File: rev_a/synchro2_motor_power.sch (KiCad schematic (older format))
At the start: 39 parts, among them U10 OPTOISOLATOR2, U11 OPTOISOLATOR2, U12 74XX74, U13 L298, U14 L298, U15 MCP48X2, U16 MCP6542, U7 LM2931, U8 SI8420, U9 SI8420

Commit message: Rev. A is pretty close to being ready.
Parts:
- added TP10: DAC_AOUT, symbol TEST_POINT
- added TP11: TWEN, symbol TEST_POINT
- added TP12: TW_SEN, symbol TEST_POINT
- added TP4: PWM_CLK, symbol TEST_POINT
- added TP5: MPWR, symbol TEST_POINT
- added TP6: MGND, symbol TEST_POINT
- added TP7: DAC_SDI, symbol TEST_POINT
- added TP8: DAC_SCK, symbol TEST_POINT
- added TP9: DAC_CS, symbol TEST_POINT
- C13: renamed from C12; value C -> 22uF
- C18: renamed from C17; value .uF -> .1uF
- U10, U11: value OPTOISOLATOR2 -> ELD207
- renumbered C13 to C14, C14 to C15, C15 to C16, C16 to C17, C18 to C19, C19 to C20, C20 to C21, N4 to N5, N5 to N6
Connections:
- net MB_MGND: now also TP6.1 (TESTPOINT)
- net MB_MPWR: now also TP5.1 (TESTPOINT)
- net TW_SEN: now reaches R12.2, U13.1 (CSA), U13.15 (CSB), U16.6
- net TW_SEN: now also TP12.1 (TESTPOINT)
- net TWD2: now reaches R9.1, U10.6, U13.10 (IN3), U13.7 (IN2)
- net TWEN: now reaches U12.9, U13.11 (EN1), U13.6 (EN2)
- net TWEN: now also TP11.1 (TESTPOINT)
- net TWD1: now reaches R7.1, U10.8, U13.12 (IN4), U13.5 (IN1)
- net TW-: now reaches D2.2 (CATHODE), D3.1 (ANODE), N5.2 (-), U13.13 (OUT3), U13.3 (OUT2)
- net TW+: now reaches D6.2 (CATHODE), D7.1 (ANODE), N5.1 (+), U13.14 (OUT4), U13.2 (OUT1)
- net DR_SEN: now reaches R11.2, U14.1 (CSA), U14.15 (CSB), U16.2
- net DRD2: now reaches R10.1, U11.6, U14.10 (IN3), U14.7 (IN2)
- net DREN: now reaches U12.5, U14.11 (EN1), U14.6 (EN2)
- net DRD1: now reaches R8.1, U11.8, U14.12 (IN4), U14.5 (IN1)
- net DR-: now reaches D4.2 (CATHODE), D5.1 (ANODE), N6.2 (-), U14.13 (OUT3), U14.3 (OUT2)
- net DR+: now reaches D8.2 (CATHODE), D9.1 (ANODE), N6.1 (+), U14.14 (OUT4), U14.2 (OUT1)
- net at U15.8 (VOUTA), U16.5: now also TP10.1 (TESTPOINT)
- net at U12.11, U12.3, U8.7 (B1): now also TP4.1 (TESTPOINT)
- net at U15.2 (~CS), U8.6 (B2): now also TP9.1 (TESTPOINT)
- net at U15.3 (SCK), U9.7 (B1): now also TP8.1 (TESTPOINT)
- net at U15.4 (SDI), U9.6 (B2): now also TP7.1 (TESTPOINT)
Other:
- note added: "+\n"
- note added: "35V Alum."
- note added: "6.3V Tant."
- note added: "AVX: TAJA226K006RNJ"
- note added: "KMet: EEV226M035A9DAA"
- moved on the sheet: N5, N6, R12

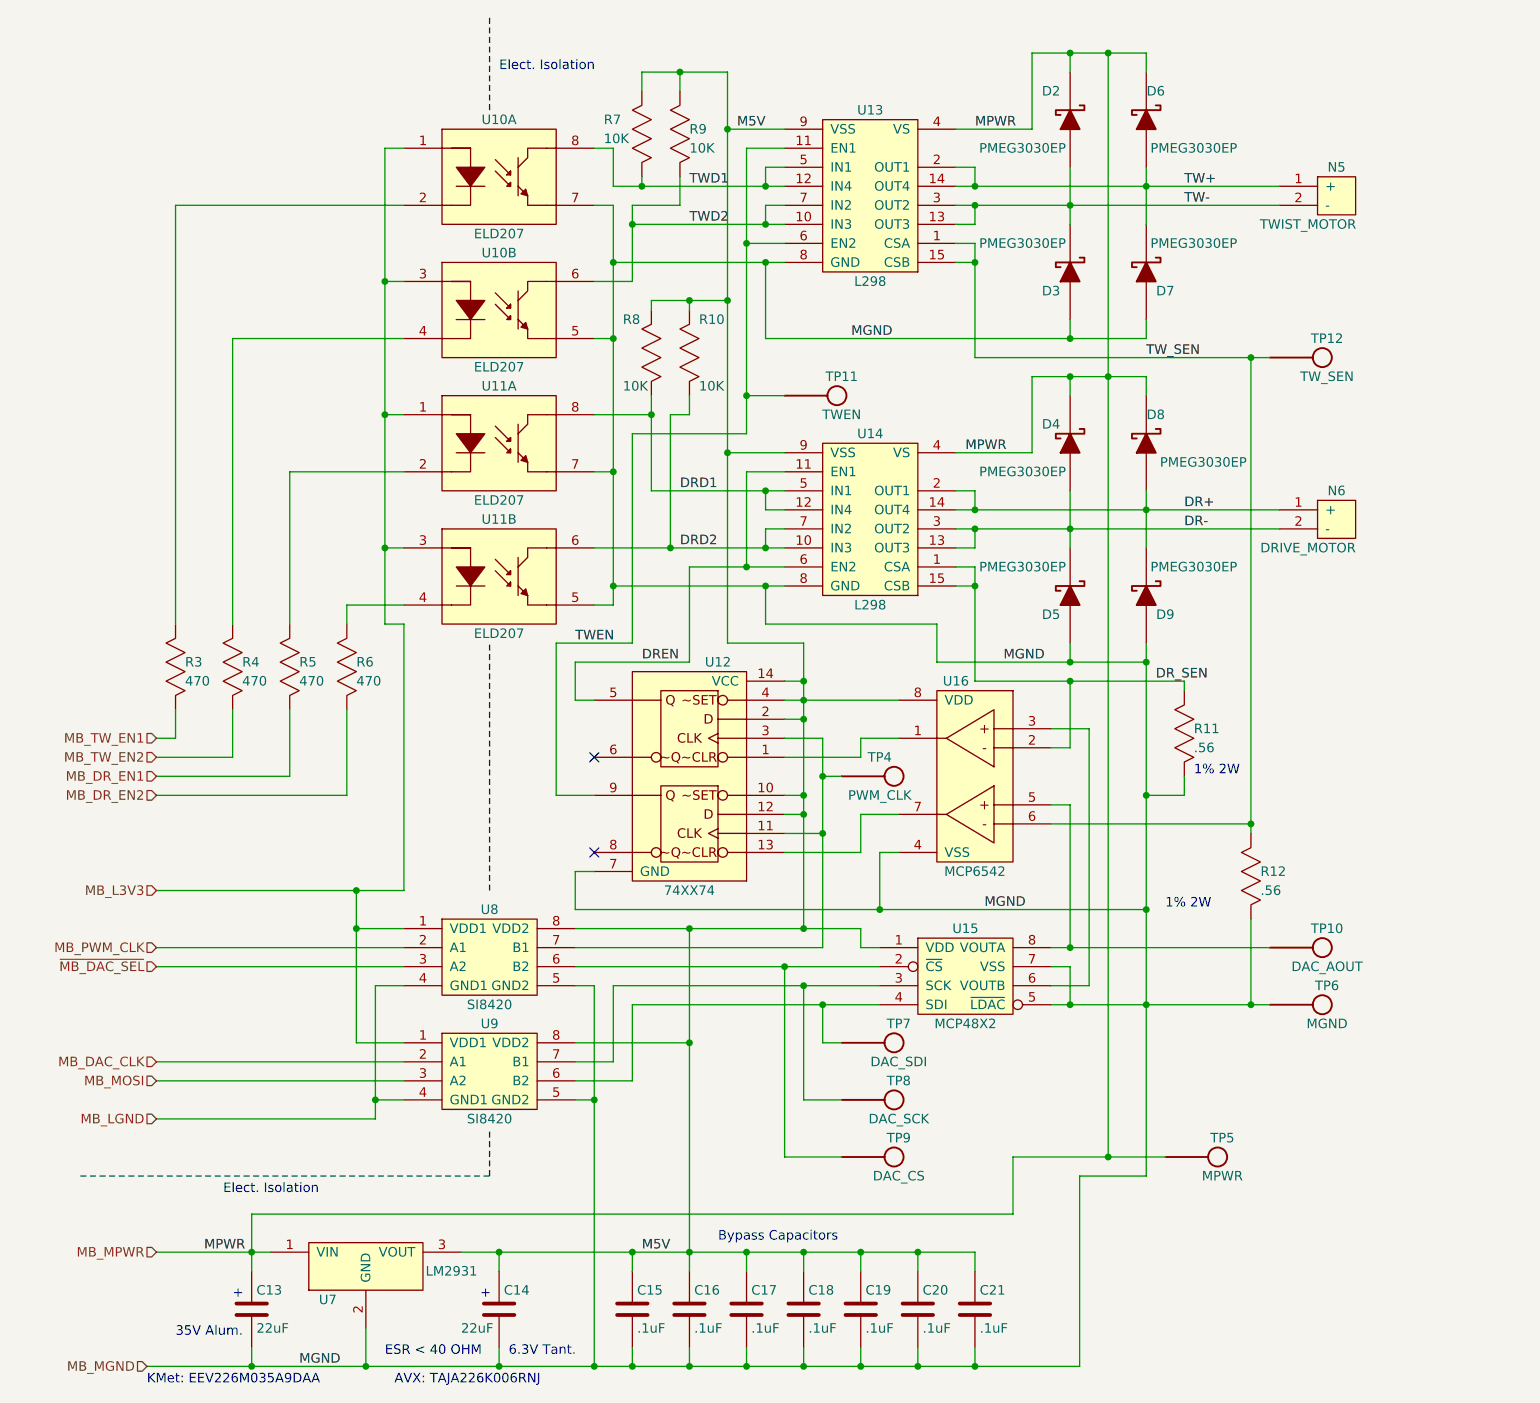
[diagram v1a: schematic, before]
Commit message: Tweak compennt values to match pricing database.  No footprints were changed.
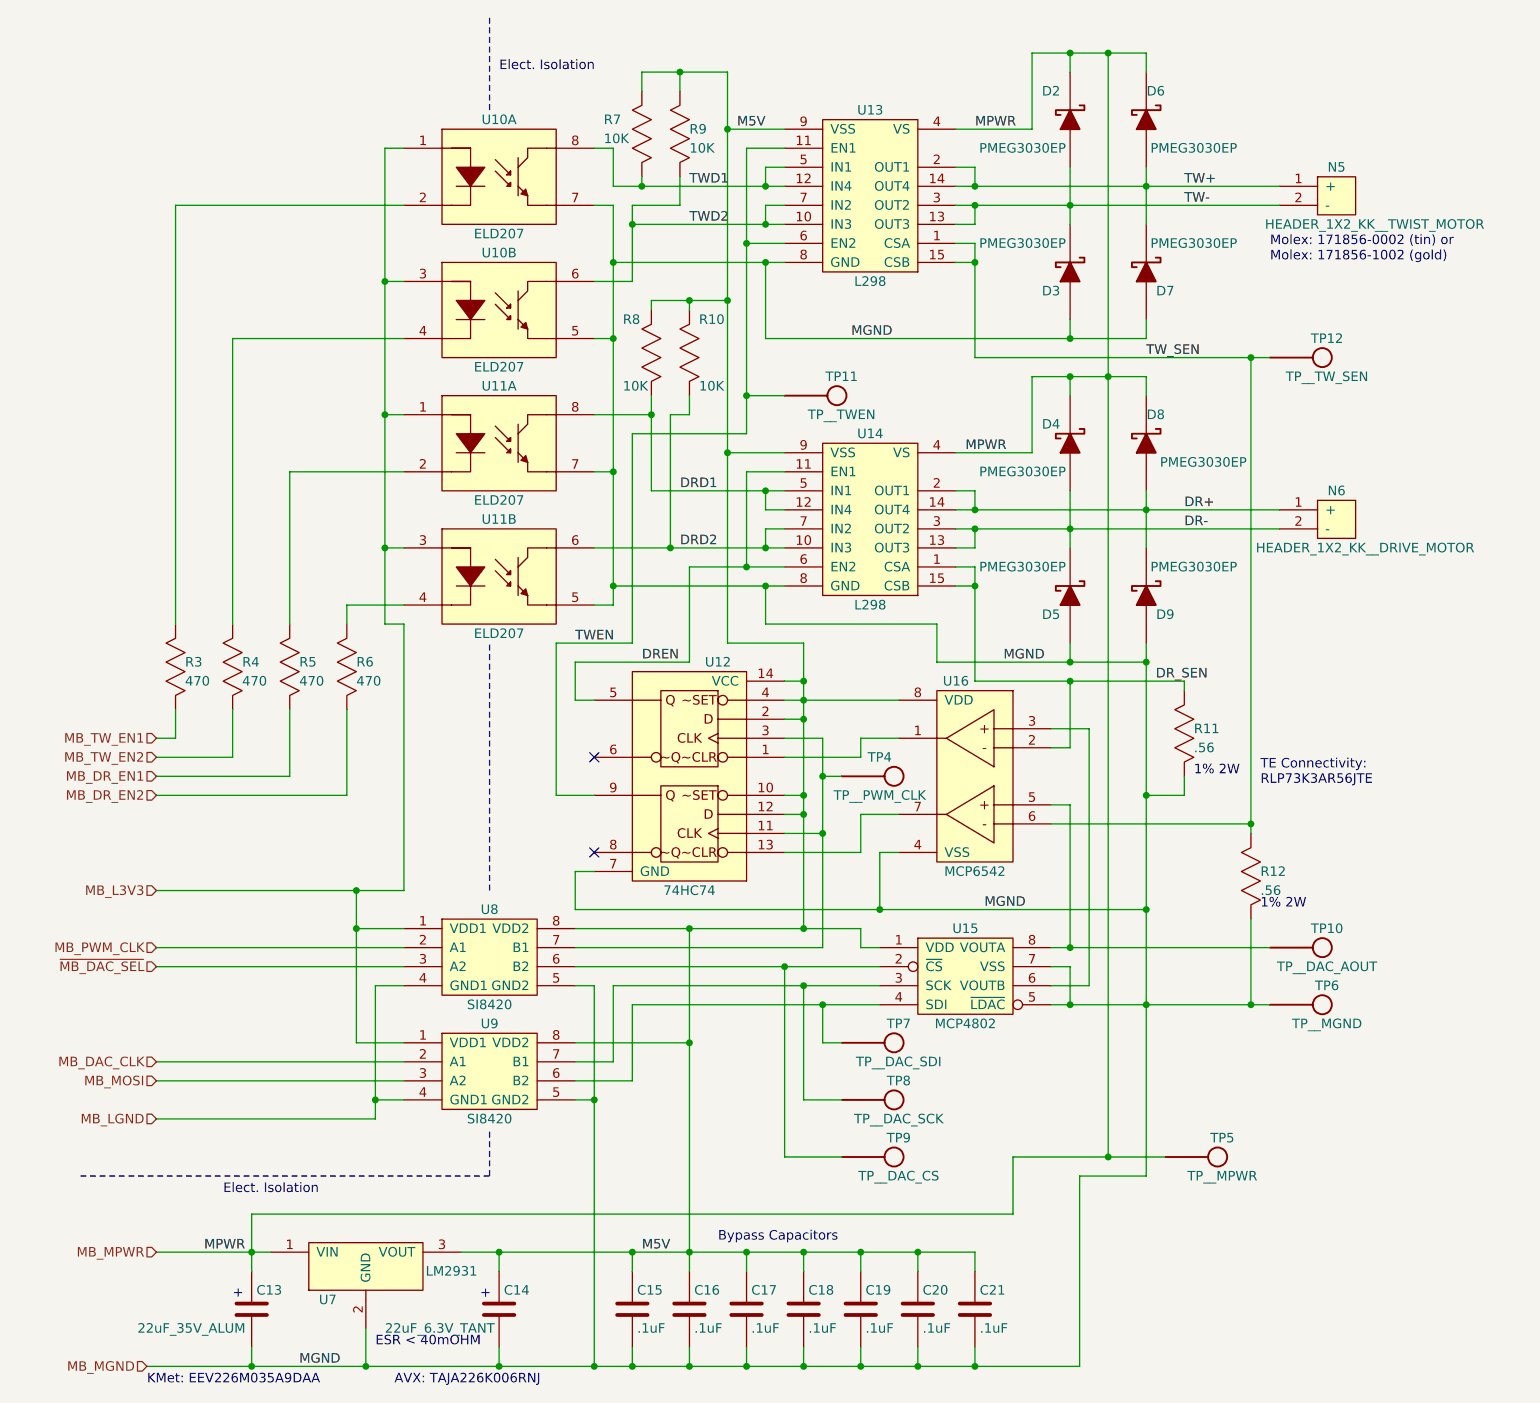
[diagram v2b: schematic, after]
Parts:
- C13: value 22uF -> 22uF_35V_ALUM
- C14: value 22uF -> 22uF_6.3V_TANT
- N5: value TWIST_MOTOR -> HEADER_1X2_KK__TWIST_MOTOR
- N6: value DRIVE_MOTOR -> HEADER_1X2_KK__DRIVE_MOTOR
- TP10: value DAC_AOUT -> TP__DAC_AOUT
- TP11: value TWEN -> TP__TWEN
- TP12: value TW_SEN -> TP__TW_SEN
- TP4: value PWM_CLK -> TP__PWM_CLK
- TP5: value MPWR -> TP__MPWR
- TP6: value MGND -> TP__MGND
- TP7: value DAC_SDI -> TP__DAC_SDI
- TP8: value DAC_SCK -> TP__DAC_SCK
- TP9: value DAC_CS -> TP__DAC_CS
- U12: value 74XX74 -> 74HC74
- U15: value MCP48X2 -> MCP4802
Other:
- note added: "ESR < 40mOHM"
- note added: "Molex: 171856-0002 (tin) or\nMolex: 171856-1002 (gold)"
- note added: "TE Connectivity:\nRLP73K3AR56JTE"
- note removed: "35V Alum."
- note removed: "6.3V Tant."
- note removed: "ESR < 40 OHM"
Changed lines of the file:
@@
 P 3900 4600
 F 0 "U12" H 3750 5300 50  0000 C CNN
-F 1 "74XX74" H 3900 4100 50  0000 C CNN
+F 1 "74HC74" H 3900 4100 50  0000 C CNN
 F 2 "" H 4150 4200 60  0000 C CNN
 F 3 "" H 4150 4200 60  0000 C CNN
@@
 	1    0    0    -1
 $EndComp
-Text Notes 6400 5200 0    50   ~ 0
+Text Notes 6900 5200 0    50   ~ 0
 1% 2W
 Text Notes 6550 4500 0    50   ~ 0
@@
 P 5350 5550
 F 0 "U15" H 5350 5800 50  0000 C CNN
-F 1 "MCP48X2" H 5350 5300 50  0000 C CNN
+F 1 "MCP4802" H 5350 5300 50  0000 C CNN
 F 2 "" H 5350 5500 60  0000 C CNN
 F 3 "" H 5350 5500 60  0000 C CNN
@@
 P 7300 1450
 F 0 "N5" H 7300 1600 50  0000 C CNN
-F 1 "TWIST_MOTOR" H 7150 1300 50  0000 C CNN
+F 1 "HEADER_1X2_KK__TWIST_MOTOR" H 7500 1300 50  0000 C CNN
 F 2 "" H 7300 1450 60  0000 C CNN
 F 3 "" H 7300 1450 60  0000 C CNN
@@
 P 7300 3150
 F 0 "N6" H 7300 3300 50  0000 C CNN
-F 1 "DRIVE_MOTOR" H 7150 3000 50  0000 C CNN
+F 1 "HEADER_1X2_KK__DRIVE_MOTOR" H 7450 3000 50  0000 C CNN
 F 2 "" H 7300 3150 60  0000 C CNN
 F 3 "" H 7300 3150 60  0000 C CNN
@@
 P 1600 7300
 F 0 "C13" H 1625 7400 50  0000 L CNN
-F 1 "22uF" H 1625 7200 50  0000 L CNN
+F 1 "22uF_35V_ALUM" H 1000 7200 50  0000 L CNN
 F 2 "" H 1638 7150 30  0000 C CNN
 F 3 "" H 1600 7300 60  0000 C CNN
@@
 P 2900 7300
 F 0 "C14" H 2925 7400 50  0000 L CNN
-F 1 "22uF" H 2700 7200 50  0000 L CNN
+F 1 "22uF_6.3V_TANT" H 2300 7200 50  0000 L CNN
 F 2 "" H 2938 7150 30  0000 C CNN
 F 3 "" H 2900 7300 60  0000 C CNN
@@
 	1    0    0    -1
 $EndComp
-Text Notes 2300 7550 0    50   ~ 0
-ESR < 40 OHM
+Text Notes 2250 7500 0    50   ~ 0
+ESR < 40mOHM
 Text Label 1850 7600 0    50   ~ 0
 MGND
@@
 	3300 5900 3900 5900
 Connection ~ 3900 5900
-Text Notes 2950 7550 0    50   ~ 0
-6.3V Tant.
 Text Notes 2800 7250 0    50   ~ 0
 +\n
 Text Notes 1500 7250 0    50   ~ 0
 +\n
-Text Notes 1200 7450 0    50   ~ 0
-35V Alum.
 Text Notes 2350 7700 0    50   ~ 0
 AVX: TAJA226K006RNJ
@@
 P 7150 5700
 F 0 "TP6" H 7250 5800 50  0000 C CNN
-F 1 "MGND" H 7250 5600 50  0000 C CNN
+F 1 "TP__MGND" H 7250 5600 50  0000 C CNN
 F 2 "" H 7150 5700 60  0000 C CNN
 F 3 "" H 7150 5700 60  0000 C CNN
@@
 P 6600 6500
 F 0 "TP5" H 6700 6600 50  0000 C CNN
-F 1 "MPWR" H 6700 6400 50  0000 C CNN
+F 1 "TP__MPWR" H 6700 6400 50  0000 C CNN
 F 2 "" H 6600 6500 60  0000 C CNN
 F 3 "" H 6600 6500 60  0000 C CNN
@@
 P 4900 4500
 F 0 "TP4" H 4900 4600 50  0000 C CNN
-F 1 "PWM_CLK" H 4900 4400 50  0000 C CNN
+F 1 "TP__PWM_CLK" H 4900 4400 50  0000 C CNN
 F 2 "" H 4900 4500 60  0000 C CNN
 F 3 "" H 4900 4500 60  0000 C CNN
@@
 P 4900 5900
 F 0 "TP7" H 5000 6000 50  0000 C CNN
-F 1 "DAC_SDI" H 5000 5800 50  0000 C CNN
+F 1 "TP__DAC_SDI" H 5000 5800 50  0000 C CNN
 F 2 "" H 4900 5900 60  0000 C CNN
 F 3 "" H 4900 5900 60  0000 C CNN
@@
 P 4900 6200
 F 0 "TP8" H 5000 6300 50  0000 C CNN
-F 1 "DAC_SCK" H 5000 6100 50  0000 C CNN
+F 1 "TP__DAC_SCK" H 5000 6100 50  0000 C CNN
 F 2 "" H 4900 6200 60  0000 C CNN
 F 3 "" H 4900 6200 60  0000 C CNN
@@
 P 4900 6500
 F 0 "TP9" H 5000 6600 50  0000 C CNN
-F 1 "DAC_CS" H 5000 6400 50  0000 C CNN
+F 1 "TP__DAC_CS" H 5000 6400 50  0000 C CNN
 F 2 "" H 4900 6500 60  0000 C CNN
 F 3 "" H 4900 6500 60  0000 C CNN
@@
 P 7150 5400
 F 0 "TP10" H 7250 5500 50  0000 C CNN
-F 1 "DAC_AOUT" H 7250 5300 50  0000 C CNN
+F 1 "TP__DAC_AOUT" H 7250 5300 50  0000 C CNN
 F 2 "" H 7150 5400 60  0000 C CNN
 F 3 "" H 7150 5400 60  0000 C CNN
@@
 P 4600 2500
 F 0 "TP11" H 4700 2600 50  0000 C CNN
-F 1 "TWEN" H 4700 2400 50  0000 C CNN
+F 1 "TP__TWEN" H 4700 2400 50  0000 C CNN
 F 2 "" H 4600 2500 60  0000 C CNN
 F 3 "" H 4600 2500 60  0000 C CNN
@@
 P 7150 2300
 F 0 "TP12" H 7250 2400 50  0000 C CNN
-F 1 "TW_SEN" H 7250 2200 50  0000 C CNN
+F 1 "TP__TW_SEN" H 7250 2200 50  0000 C CNN
 F 2 "" H 7150 2300 60  0000 C CNN
 F 3 "" H 7150 2300 60  0000 C CNN
@@
 $EndComp
 Connection ~ 6850 2300
+Text Notes 6900 4550 0    50   ~ 0
+TE Connectivity:\nRLP73K3AR56JTE
+Text Notes 6950 1800 0    50   ~ 0
+Molex: 171856-0002 (tin) or\nMolex: 171856-1002 (gold)
 $EndSCHEMATC
